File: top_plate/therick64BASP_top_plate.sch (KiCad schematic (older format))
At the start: 85 parts, among them U1 HOLE, U10 HOLE, U11 HOLE, U12 HOLE, U13 HOLE, U14 HOLE, U15 HOLE, U16 HOLE, U17 HOLE, U18 HOLE, U19 HOLE, U2 HOLE, U20 HOLE, U21 HOLE, U22 HOLE, U23 HOLE, U24 HOLE, U25 HOLE, U26 HOLE, U27 HOLE, U28 HOLE, U29 HOLE, U3 HOLE, U30 HOLE, U31 HOLE, U32 HOLE, U33 HOLE, U34 HOLE, U35 HOLE, U36 HOLE, U37 HOLE, U38 HOLE, U39 HOLE, U4 HOLE, U40 HOLE, U41 HOLE, U42 HOLE, U43 HOLE, U44 HOLE, U45 HOLE, U46 HOLE, U47 HOLE, U48 HOLE, U49 HOLE, U5 HOLE, U50 HOLE, U51 HOLE, U52 HOLE, U53 HOLE, U54 HOLE, U55 HOLE, U56 HOLE, U57 HOLE, U58 HOLE, U59 HOLE, U6 HOLE, U60 HOLE, U61 HOLE, U62 HOLE, U63 HOLE, U64 HOLE, U65 HOLE, U66 HOLE, U67 HOLE, U7 HOLE, U8 HOLE, U9 HOLE

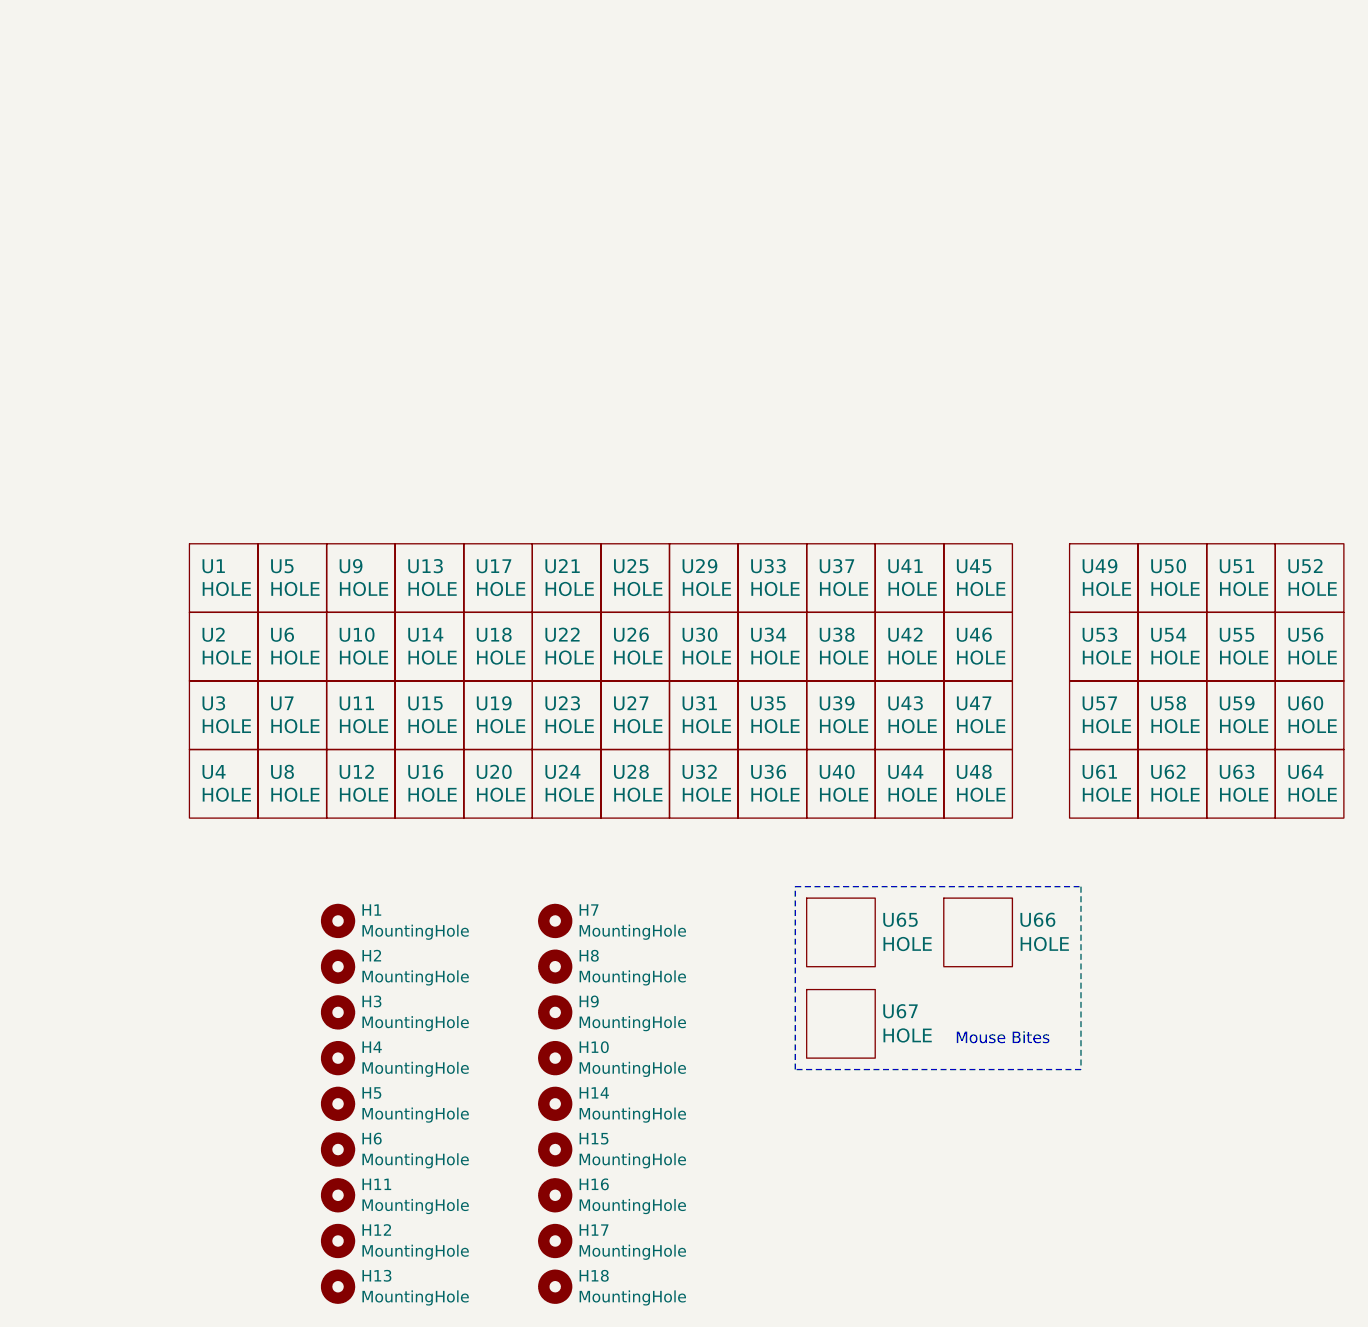
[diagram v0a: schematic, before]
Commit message: Added mounting holes
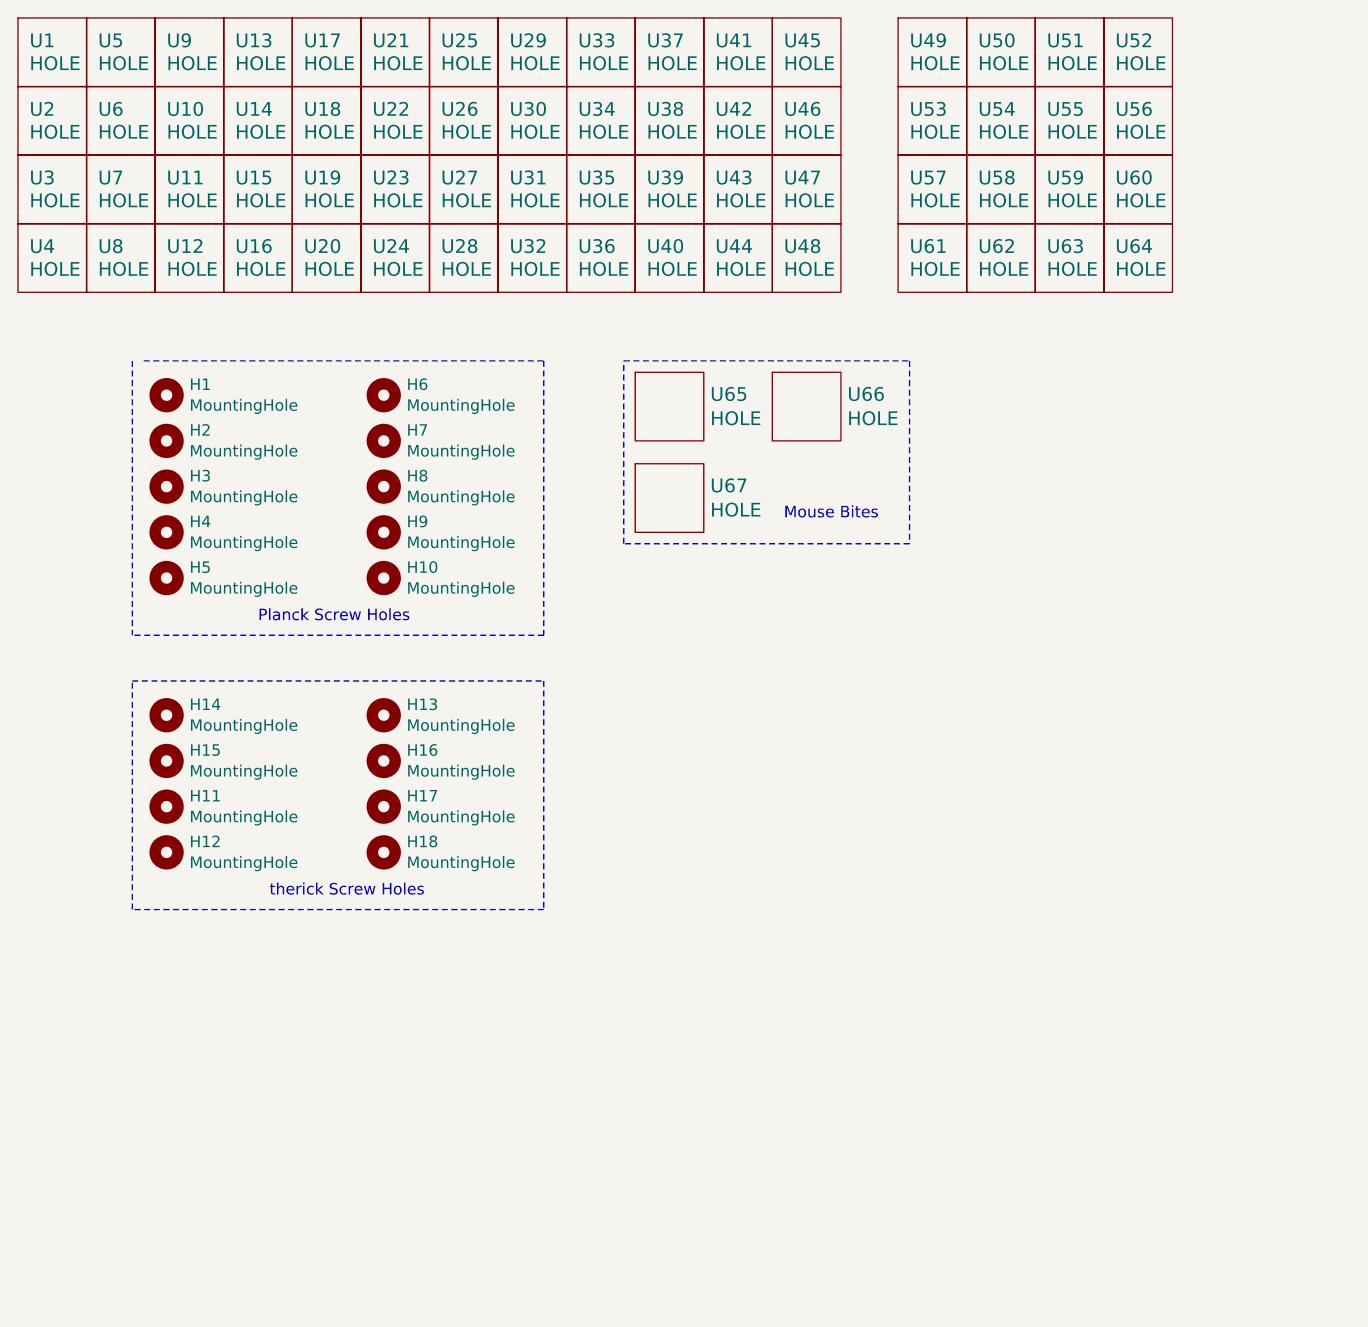
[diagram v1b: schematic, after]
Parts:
- H1, H10, H11, H12, H13, H14, H15, H16, H17, H18, H2, H3, H4, H5, H6, H7, H8, H9: footprint random-keyboard-parts:Generic-Mounthole -> random-keyboard-parts:plate_hole_4mm_tht
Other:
- note added: "Planck Screw Holes"
- note added: "therick Screw Holes"
- moved on the sheet: H1, H10, H11, H12, H13, H14, H15, H16, H17, H18, H2, H3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
